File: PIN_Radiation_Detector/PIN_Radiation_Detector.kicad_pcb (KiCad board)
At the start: 2 copper layers, 68.6 x 31.8 mm, 21 parts, among them J1 Conn_01x03, Q1 MMBF4392LT1G, U1 LM358DR

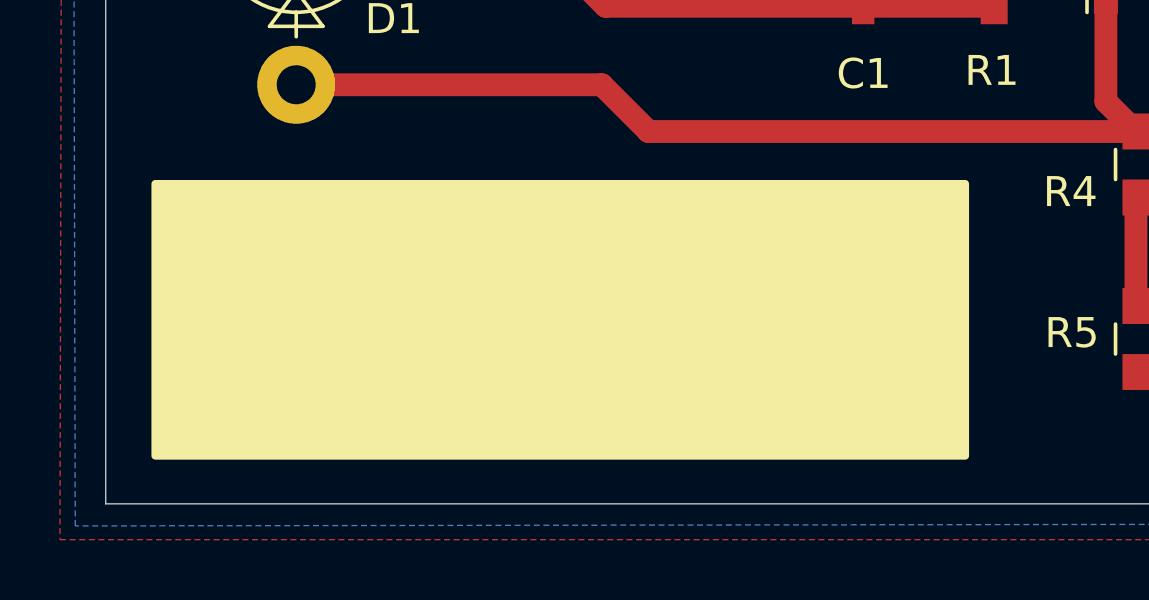
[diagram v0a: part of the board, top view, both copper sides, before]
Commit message: Fix PCB page size
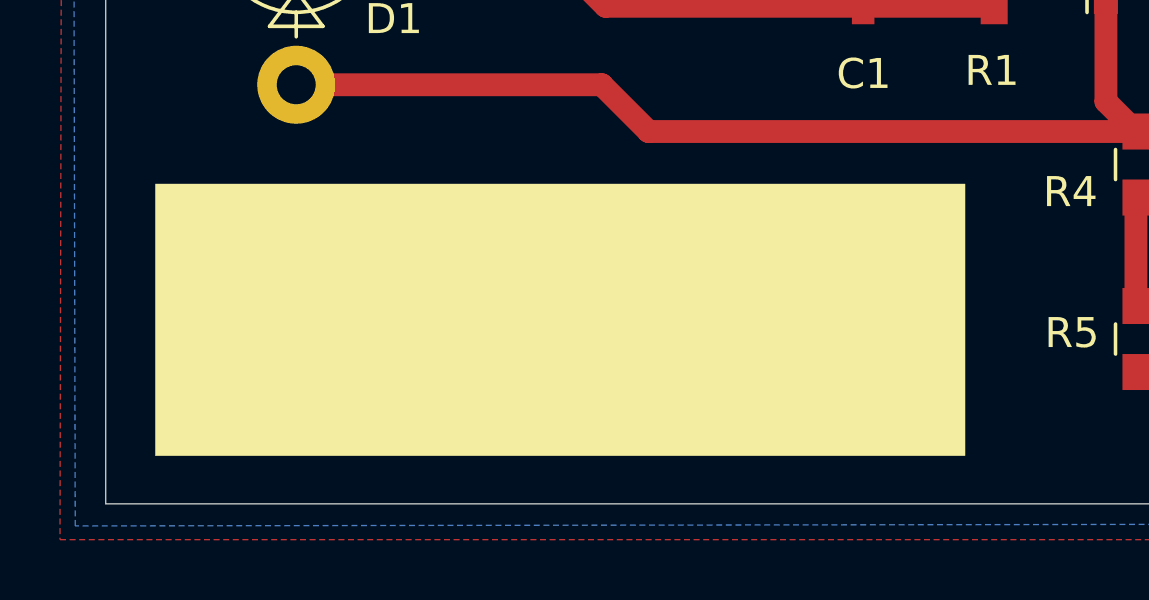
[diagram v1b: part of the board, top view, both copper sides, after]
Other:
- net class Default removed

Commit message: Fix DRC issues in PCB
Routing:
- net Net-(C7-Pad1): track 23.6 -> 22.0 mm
- net Net-(J1-Pad3): track 7.72 -> 6.52 mm
- net Net-(C6-Pad1): track 16.8 -> 15.7 mm
- net Net-(R4-Pad1): track 4.47 -> 3.62 mm
- net GND: vias 7 -> 8
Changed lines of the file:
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@@
   (via (at 192.9384 89.1286) (size 0.762) (drill 0.381) (layers "F.Cu" "B.Cu") (net 1))
   (via (at 193.7512 92.456) (size 0.762) (drill 0.381) (layers "F.Cu" "B.Cu") (net 1))
+  (via (at 181.7 91.7) (size 0.762) (drill 0.381) (layers "F.Cu" "B.Cu") (net 1))
   (segment (start 198.3232 81.534) (end 198.3232 87.6808) (width 0.254) (layer "B.Cu") (net 1))
   (segment (start 192.4558 92.456) (end 188.1124 96.7994) (width 0.254) (layer "B.Cu") (net 1))
@@
   (segment (start 181.61 101.3304) (end 181.61 97.79) (width 0.254) (layer "F.Cu") (net 3))
   (segment (start 200.66 96.52) (end 195.58 96.52) (width 0.254) (layer "F.Cu") (net 4))
-  (segment (start 186.289 93.0402) (end 185.26 93.0402) (width 0.254) (layer "F.Cu") (net 5))
   (segment (start 187.03 103.5256) (end 187.0252 103.5304) (width 0.254) (layer "F.Cu") (net 5))
-  (segment (start 187.03 99.06) (end 187.03 93.7812) (width 0.254) (layer "F.Cu") (net 5))
   (segment (start 187.03 99.06) (end 187.03 103.5256) (width 0.254) (layer "F.Cu") (net 5))
   (segment (start 181.61 103.5304) (end 187.0252 103.5304) (width 0.254) (layer "F.Cu") (net 5))
-  (segment (start 187.03 93.7812) (end 186.289 93.0402) (width 0.254) (layer "F.Cu") (net 5))
-  (segment (start 189.23 93.0656) (end 189.2046 93.0402) (width 0.254) (layer "F.Cu") (net 6))
+  (segment (start 187.03 99.06) (end 186.7 98.73) (width 0.254) (layer "F.Cu") (net 5))
+  (segment (start 186.7 98.73) (end 186.7 93.4512) (width 0.254) (layer "F.Cu") (net 5))
+  (segment (start 186.289 93.0402) (end 185.26 93.0402) (width 0.254) (layer "F.Cu") (net 5))
+  (segment (start 186.7 93.4512) (end 186.289 93.0402) (width 0.254) (layer "F.Cu") (net 5))
   (segment (start 185.735 90.5002) (end 188.275 93.0402) (width 0.254) (layer "F.Cu") (net 6))
-  (segment (start 189.23 99.06) (end 189.23 93.0656) (width 0.254) (layer "F.Cu") (net 6))
-  (segment (start 189.23 99.06) (end 189.23 100.4316) (width 0.254) (layer "F.Cu") (net 6))
-  (segment (start 189.631 93.0402) (end 190.66 93.0402) (width 0.254) (layer "F.Cu") (net 6))
-  (segment (start 190.185 93.0402) (end 190.66 93.0402) (width 0.254) (layer "F.Cu") (net 6))
+  (segment (start 189.23 99.06) (end 189.23 103.2256) (width 0.254) (layer "F.Cu") (net 6))
+  (segment (start 189.2046 94.4958) (end 189.2046 93.0402) (width 0.254) (layer "F.Cu") (net 6))
+  (segment (start 189.23 103.2256) (end 188.9252 103.5304) (width 0.254) (layer "F.Cu") (net 6))
   (segment (start 188.275 93.0402) (end 189.2046 93.0402) (width 0.254) (layer "F.Cu") (net 6))
-  (segment (start 189.23 100.4316) (end 188.9252 100.7364) (width 0.254) (layer "F.Cu") (net 6))
+  (segment (start 189.2046 93.0402) (end 190.66 93.0402) (width 0.254) (layer "F.Cu") (net 6))
+  (segment (start 189.23 99.06) (end 189.7 98.59) (width 0.254) (layer "F.Cu") (net 6))
+  (segment (start 189.7 98.59) (end 189.7 94.9912) (width 0.254) (layer "F.Cu") (net 6))
   (segment (start 185.26 90.5002) (end 185.735 90.5002) (width 0.254) (layer "F.Cu") (net 6))
-  (segment (start 188.9252 100.7364) (end 188.9252 103.5304) (width 0.254) (layer "F.Cu") (net 6))
-  (segment (start 189.2046 93.0402) (end 189.631 93.0402) (width 0.254) (layer "F.Cu") (net 6))
+  (segment (start 189.7 94.9912) (end 189.2046 94.4958) (width 0.254) (layer "F.Cu") (net 6))
   (segment (start 200.66 88.9) (end 195.58 88.9) (width 0.254) (layer "F.Cu") (net 7))
   (segment (start 205.74 88.9) (end 200.66 88.9) (width 0.254) (layer "F.Cu") (net 7))
@@
   (segment (start 195.58 94.32) (end 195.58 91.1) (width 0.254) (layer "F.Cu") (net 8))
   (segment (start 172.88 83.82) (end 172.88 88.1402) (width 0.762) (layer "F.Cu") (net 9))
-  (segment (start 172.88 83.82) (end 173.83 83.82) (width 0.254) (layer "F.Cu") (net 9))
   (segment (start 178.14 83.82) (end 172.88 83.82) (width 0.762) (layer "F.Cu") (net 9))
   (segment (start 171.8626 89.17) (end 171.8564 89.1638) (width 0.254) (layer "F.Cu") (net 9))
   (segment (start 172.88 88.1402) (end 171.8564 89.1638) (width 0.762) (layer "F.Cu") (net 9))
   (segment (start 176.53 89.17) (end 171.8626 89.17) (width 0.254) (layer "F.Cu") (net 9))
-  (segment (start 177.99 83.82) (end 178.14 83.82) (width 0.254) (layer "F.Cu") (net 9))
-  (segment (start 190.66 90.5002) (end 190.66 88.27) (width 0.762) (layer "F.Cu") (net 10))
+  (segment (start 190.66 88.27) (end 190.66 89.4382) (width 0.762) (layer "F.Cu") (net 10))
   (segment (start 193.7382 86.36) (end 190.66 89.4382) (width 0.762) (layer "F.Cu") (net 10))
   (segment (start 186.21 83.82) (end 185.26 83.82) (width 0.762) (layer "F.Cu") (net 10))
-  (segment (start 190.66 90.5002) (end 190.185 90.5002) (width 0.254) (layer "F.Cu") (net 10))
+  (segment (start 190.66 89.4382) (end 190.66 90.5002) (width 0.762) (layer "F.Cu") (net 10))
   (segment (start 190.66 88.27) (end 186.21 83.82) (width 0.762) (layer "F.Cu") (net 10))
   (segment (start 185.26 83.82) (end 180.34 83.82) (width 0.762) (layer "F.Cu") (net 10))
   (segment (start 197.02 86.36) (end 193.7382 86.36) (width 0.762) (layer "F.Cu") (net 10))
-  (segment (start 190.66 89.4382) (end 190.66 90.5002) (width 0.762) (layer "F.Cu") (net 10))
   (segment (start 160.3346 95.5392) (end 176.5808 95.5392) (width 0.762) (layer "F.Cu") (net 11))
   (segment (start 158.7754 93.98) (end 160.3346 95.5392) (width 0.762) (layer "F.Cu") (net 11))
   (segment (start 175.58 91.17) (end 175.58 94.5384) (width 0.762) (layer "F.Cu") (net 11))
-  (segment (start 176.5808 95.3892) (end 176.5808 95.5392) (width 0.254) (layer "F.Cu") (net 11))
   (segment (start 148.59 93.98) (end 158.7754 93.98) (width 0.762) (layer "F.Cu") (net 11))
   (segment (start 175.58 94.5384) (end 176.5808 95.5392) (width 0.762) (layer "F.Cu") (net 11))
@@
   (segment (start 184.1602 91.7702) (end 184.231 91.7702) (width 0.254) (layer "F.Cu") (net 12))
   (segment (start 176.5808 97.7392) (end 176.5808 101.3558) (width 0.762) (layer "F.Cu") (net 13))
-  (segment (start 176.5808 101.3558) (end 176.5808 100.5018) (width 0.254) (layer "F.Cu") (net 13))
   (segment (start 205.74 86.36) (end 199.22 86.36) (width 0.762) (layer "F.Cu") (net 14))
-  (segment (start 205.74 86.36) (end 204.537919 86.36) (width 0.254) (layer "F.Cu") (net 14))
   (zone (net 1) (net_name "GND") (layer "F.Cu") (hatch edge 0.508)
     (connect_pads (clearance 0.508))
